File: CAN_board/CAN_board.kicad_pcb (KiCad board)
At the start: 2 copper layers, 67.3 x 67.3 mm, 7 parts, among them J1 Conn_02x20_Odd_Even_Rasbpi, J2 Conn_02x20_Odd_Even_extra, J3 Converter, J4 MCP2515, J5 Battery, J6 Conn_01x02_Male, J7 OBD_connector

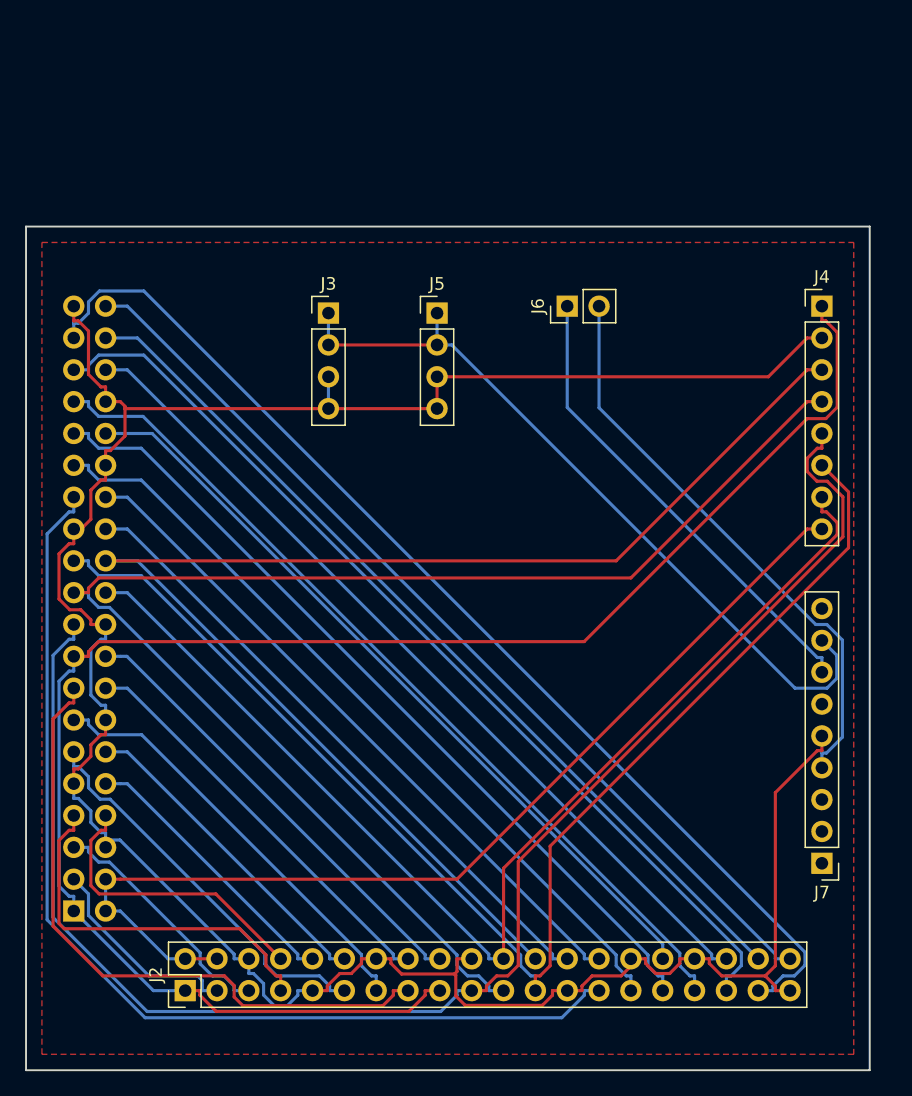
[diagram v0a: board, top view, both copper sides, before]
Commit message: Components placed, routing to be done
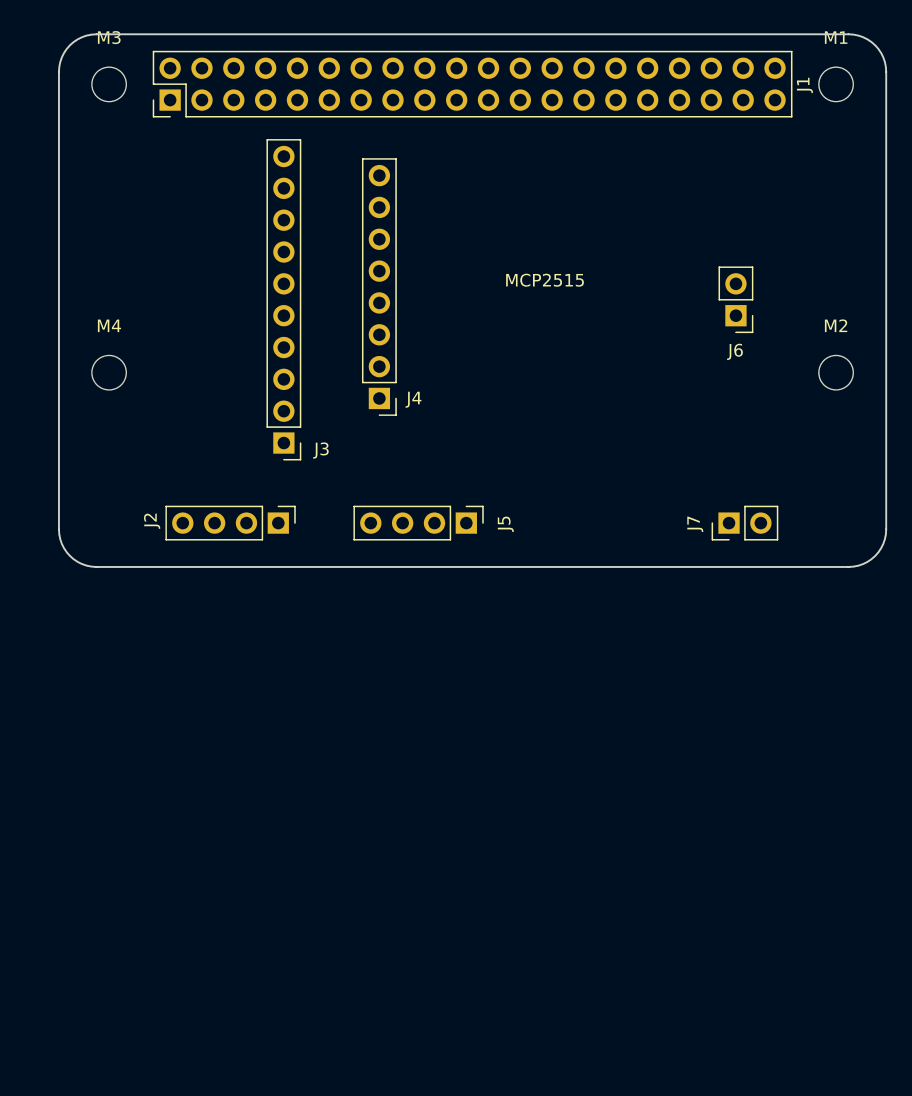
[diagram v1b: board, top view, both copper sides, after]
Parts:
- added M1: MountingHole_2.75mm, MountingHole:MountingHole_2.7mm, F.Cu at (167.5, 42.0)
- added M2: MountingHole_2.75mm, MountingHole:MountingHole_2.7mm, F.Cu at (167.5, 65.0)
- added M3: MountingHole_2.75mm, MountingHole:MountingHole_2.7mm, F.Cu at (109.5, 42.0)
- added M4: MountingHole_2.75mm, MountingHole:MountingHole_2.7mm, F.Cu at (109.5, 65.0)
- J1: moved to F.Cu
- J2: value Conn_02x20_Odd_Even_extra -> Sensor input; footprint Connector_PinHeader_2.54mm:PinHeader_2x20_P2.54mm_Vertical -> Connector_PinHeader_2.54mm:PinHeader_1x04_P2.54mm_Vertical
- J3: value Converter -> ADS1115; footprint Connector_PinHeader_2.54mm:PinHeader_1x04_P2.54mm_Vertical -> Connector_PinHeader_2.54mm:PinHeader_1x10_P2.54mm_Vertical
- J7: value OBD_connector -> Conn_01x02_Male; footprint Connector_PinHeader_2.54mm:PinHeader_1x09_P2.54mm_Vertical -> Connector_PinHeader_2.54mm:PinHeader_1x02_P2.54mm_Vertical
- moved J1 65.2 mm to (114.4, 43.2), turned to 90 degrees
- moved J2 38.0 mm to (123.0, 77.0), turned to 270 degrees
- moved J4 36.1 mm to (131.1, 67.1), turned to 180 degrees
- moved J7 28.1 mm to (159.0, 77.0), turned to 90 degrees
- moved J5 16.9 mm to (138.0, 77.0), turned to 270 degrees
- moved J6 13.5 mm to (159.5, 60.5), turned to 180 degrees
- moved J3 11.0 mm to (123.4, 70.6), turned to 180 degrees
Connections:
- J1 pad 10: /10 -> (no net)
- J1 pad 11: /11 -> /ALRT
- J1 pad 12: /12 -> (no net)
- J1 pad 13: /13 -> (no net)
- J1 pad 15: /15 -> (no net)
- J1 pad 16: /16 -> (no net)
- J1 pad 17: /3V3 -> (no net)
- J1 pad 18: /18 -> (no net)
- J1 pad 26: /26 -> (no net)
- J1 pad 27: /27 -> (no net)
- J1 pad 28: /28 -> (no net)
- J1 pad 29: /29 -> (no net)
- J1 pad 3: /3 -> /SDA
- J1 pad 31: /31 -> (no net)
- J1 pad 32: /32 -> (no net)
- J1 pad 33: /33 -> (no net)
- J1 pad 35: /35 -> (no net)
- J1 pad 36: /36 -> (no net)
- J1 pad 37: /37 -> (no net)
- J1 pad 38: /38 -> (no net)
- J1 pad 4: /5V -> (no net)
- J1 pad 40: /40 -> (no net)
- J1 pad 5: /5 -> /SCL
- J1 pad 7: /7 -> (no net)
- J1 pad 8: /8 -> (no net)
- J2 pad 1: /3V3 -> /A0
- J2 pad 2: /5V -> /A1
- J2 pad 3: /3 -> /A2
- J2 pad 4: /5V -> /A3
- J3 pad 1: /12V -> /3V3
- J3 pad 2: /12V -> /GND
- J3 pad 3: /GND -> /SCL
- J3 pad 4: /GND -> /SDA
- J5 pad 1: /12V -> /5V
- J5 pad 2: /12V -> /3V3
- J7 pad 1: Net-(J7-Pad1) -> /CANH
- J7 pad 2: Net-(J7-Pad2) -> /CANL
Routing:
- net /GND: track 214.1 -> 0.00 mm
- net /3V3: track 133.5 -> 0.00 mm
- net /MOSI: track 122.0 -> 0.00 mm
- net /MISO: track 114.6 -> 0.00 mm
- net /CS: track 110.9 -> 0.00 mm
- net /SCLK: track 105.8 -> 0.00 mm
- net /INT: track 92.6 -> 0.00 mm
- net /37: track 88.8 -> 0.00 mm
- net /27: track 83.2 -> 0.00 mm
- net /5V: track 81.7 -> 0.00 mm
- net /35: track 77.5 -> 0.00 mm
- net /40: track 76.4 -> 0.00 mm
- net /38: track 72.6 -> 0.00 mm
- net /33: track 70.5 -> 0.00 mm
- net /36: track 69.2 -> 0.00 mm
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- removed copper zone on F.Cu, net /GND
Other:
- board size 67.3 x 67.3 mm -> 66 x 42.5 mm
- net class Default: clearance 0.2 -> 0.5; trace_width 0.25 -> 0.5
- net class Thick_2 added: clearance 0.5, trace_width 1, via_dia 0.8, via_drill 0.4
- rule trace_clearance: 0.2 -> 0.5
- board text added: "MCP2515"
